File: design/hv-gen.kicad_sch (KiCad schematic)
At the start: 30 parts, among them Q1 Q_NMOS_DGS, Q2 2SA1213, T1 DA2033-AL, U8 TLP152TPL_E

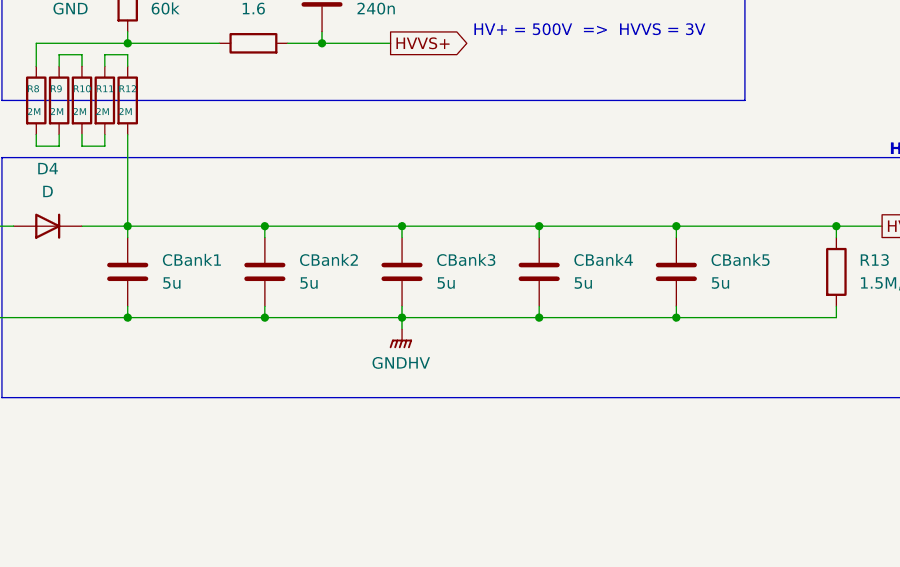
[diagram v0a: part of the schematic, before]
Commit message: fixed component value typo
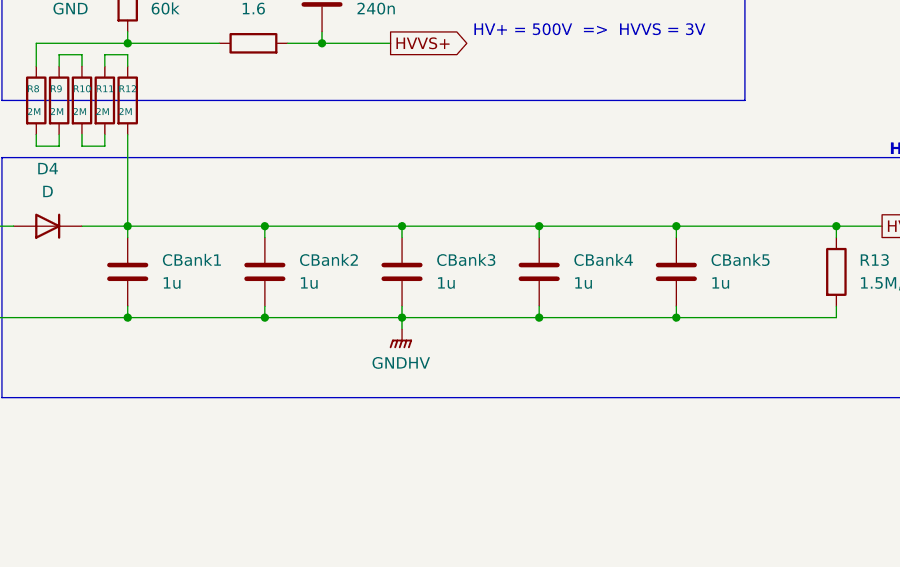
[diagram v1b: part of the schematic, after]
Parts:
- CBank1, CBank2, CBank3, CBank4, CBank5: value 5u -> 1u

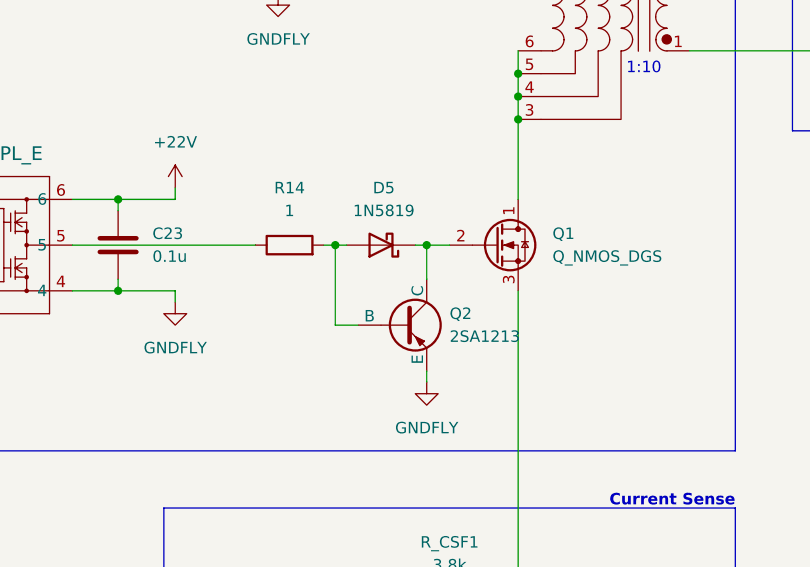
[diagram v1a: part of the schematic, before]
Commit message: Fixed PNP turnoff circuit, increased measurement buffer spacing
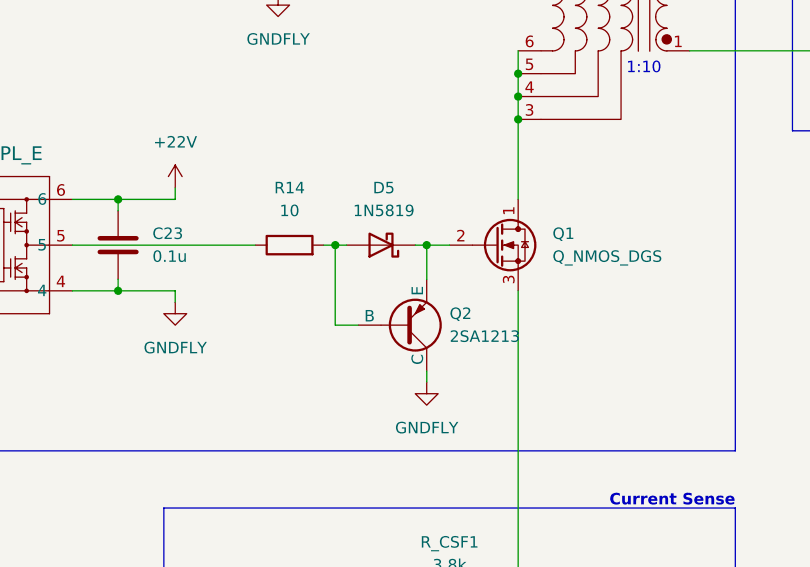
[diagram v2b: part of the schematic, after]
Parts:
- R14: value 1 -> 10; footprint Resistor_SMD:R_0603_1608Metric -> Resistor_SMD:R_0805_2012Metric
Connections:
- net GNDFLY: now also Q2.C; no longer Q2.E
- net at D5.1 (K), Q1.2 (G): now also Q2.E; no longer Q2.C

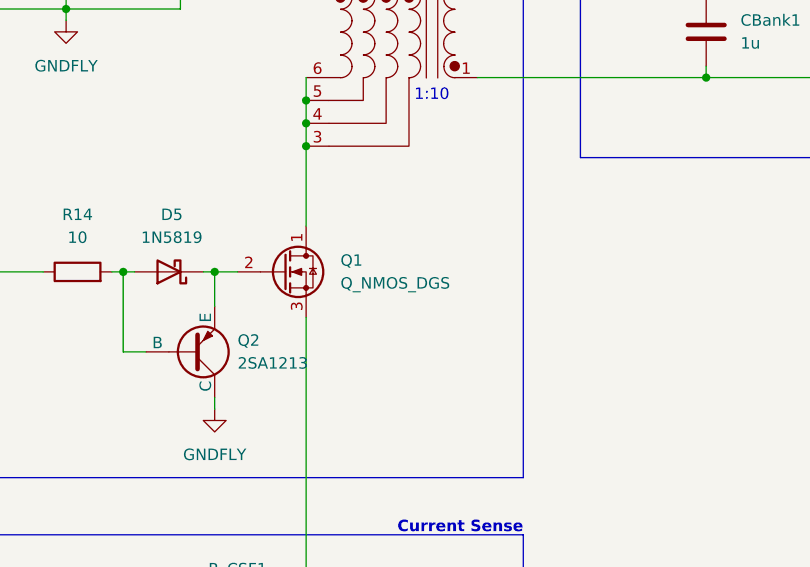
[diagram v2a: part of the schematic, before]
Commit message: corrected Q1 footprint and orientation
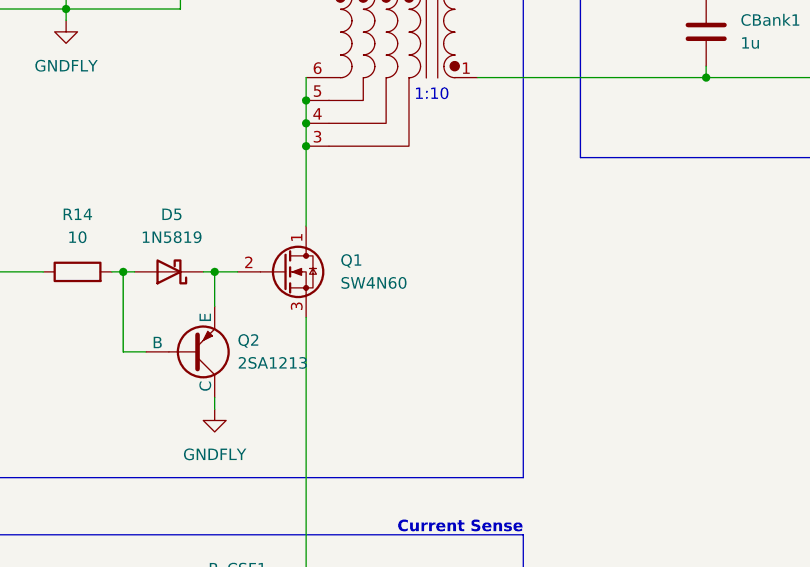
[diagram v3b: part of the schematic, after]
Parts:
- Q1: value Q_NMOS_DGS -> SW4N60; footprint Package_TO_SOT_SMD:TO-252-2 -> project-footprints:SW4N60

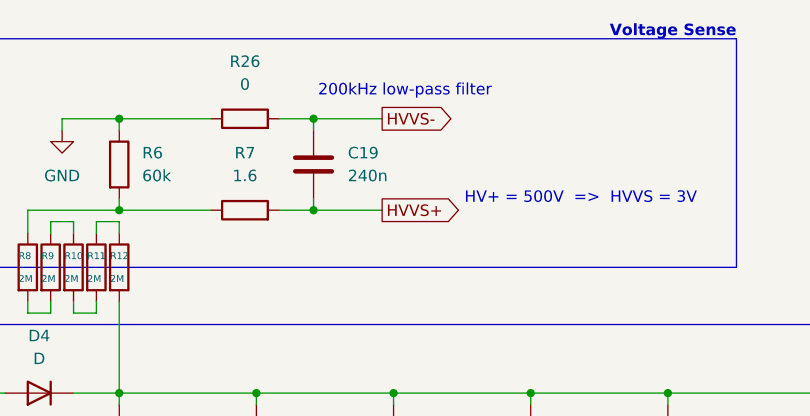
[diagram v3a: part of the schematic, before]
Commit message: Reduced HVVS filter capacitance
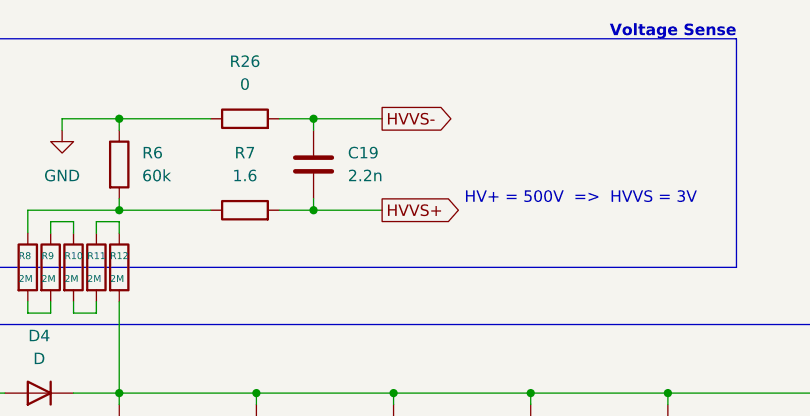
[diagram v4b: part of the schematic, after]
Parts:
- C19: value 240n -> 2.2n
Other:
- note removed: "200kHz low-pass filter"

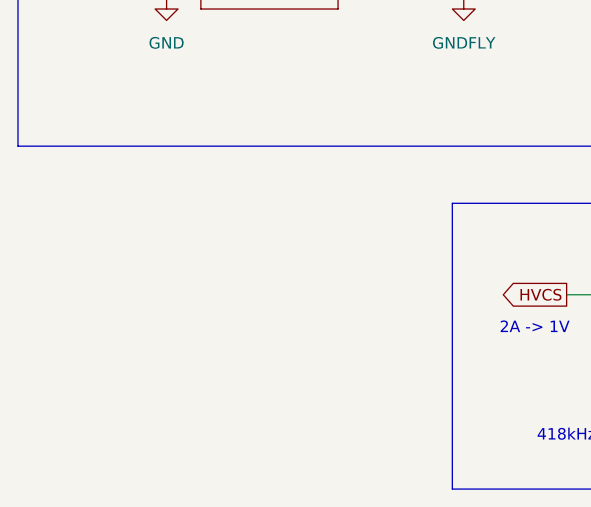
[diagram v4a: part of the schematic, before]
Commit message: Modified high voltage gate drive circuit and layout, added net tie from GND to flyback converter GND
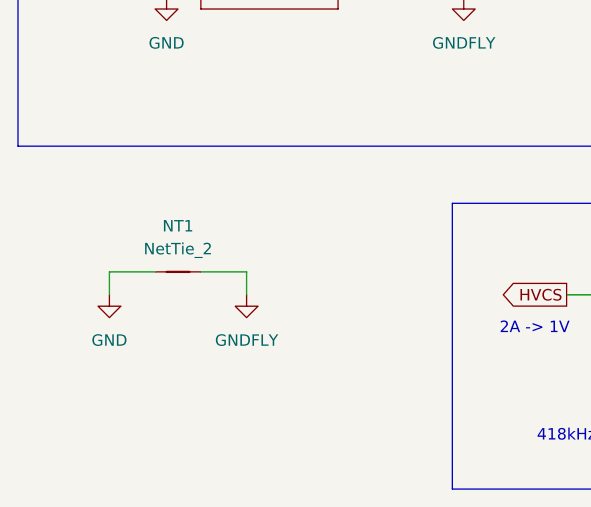
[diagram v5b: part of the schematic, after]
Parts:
- added NT1: NetTie_2, NetTie:NetTie-2_SMD_Pad2.0mm, symbol Device:NetTie_2
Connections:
- net GND: now also NT1.1
- net GNDFLY: now also NT1.2

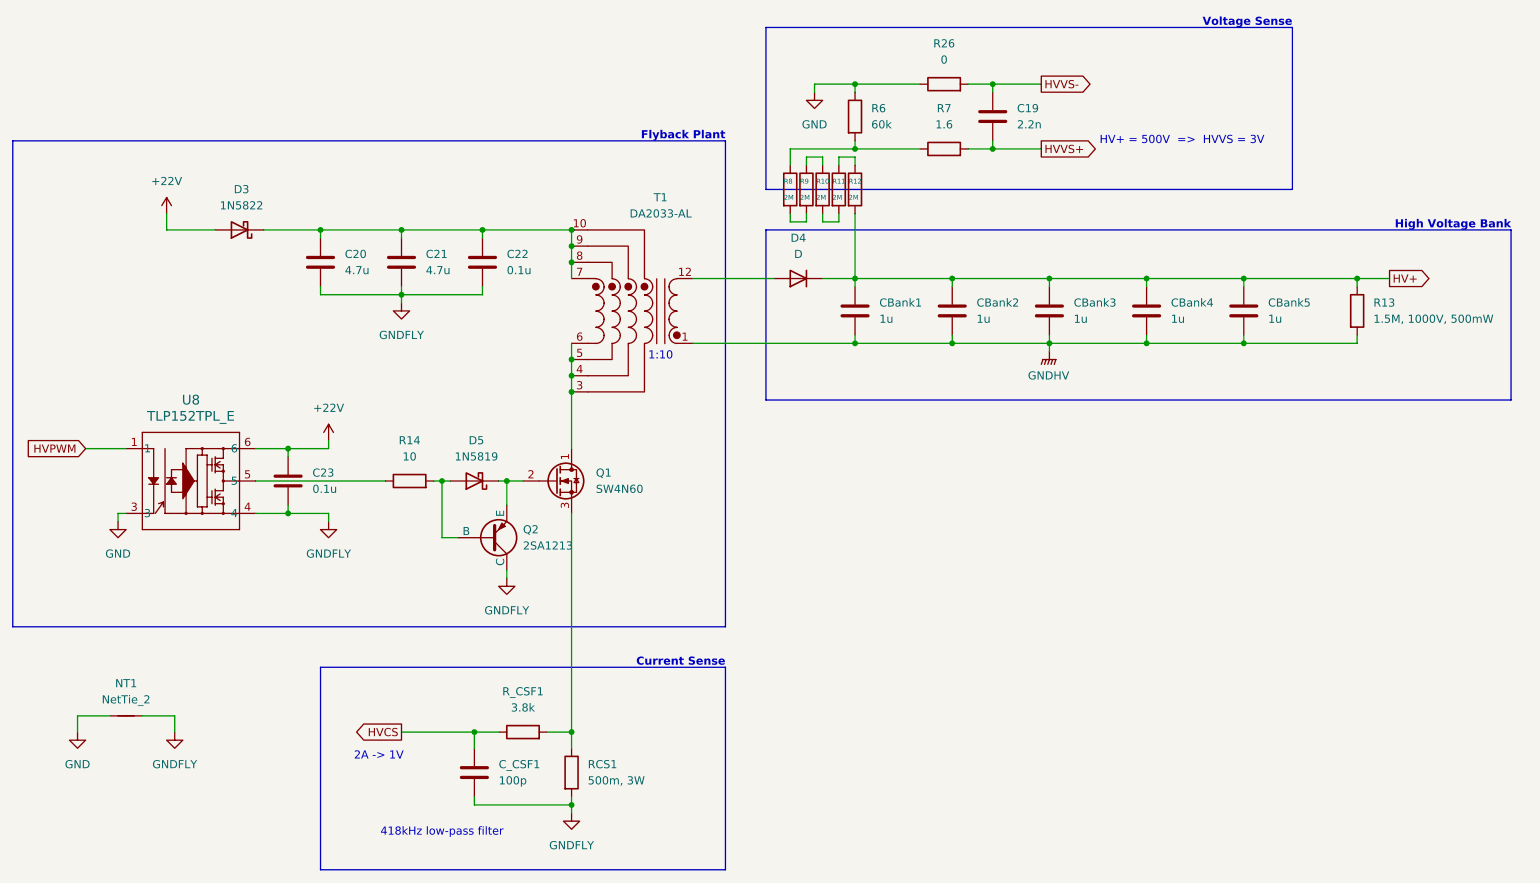
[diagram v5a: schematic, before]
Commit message: Altered HVCS filter, replaced some high current traces with filled zones, added labels
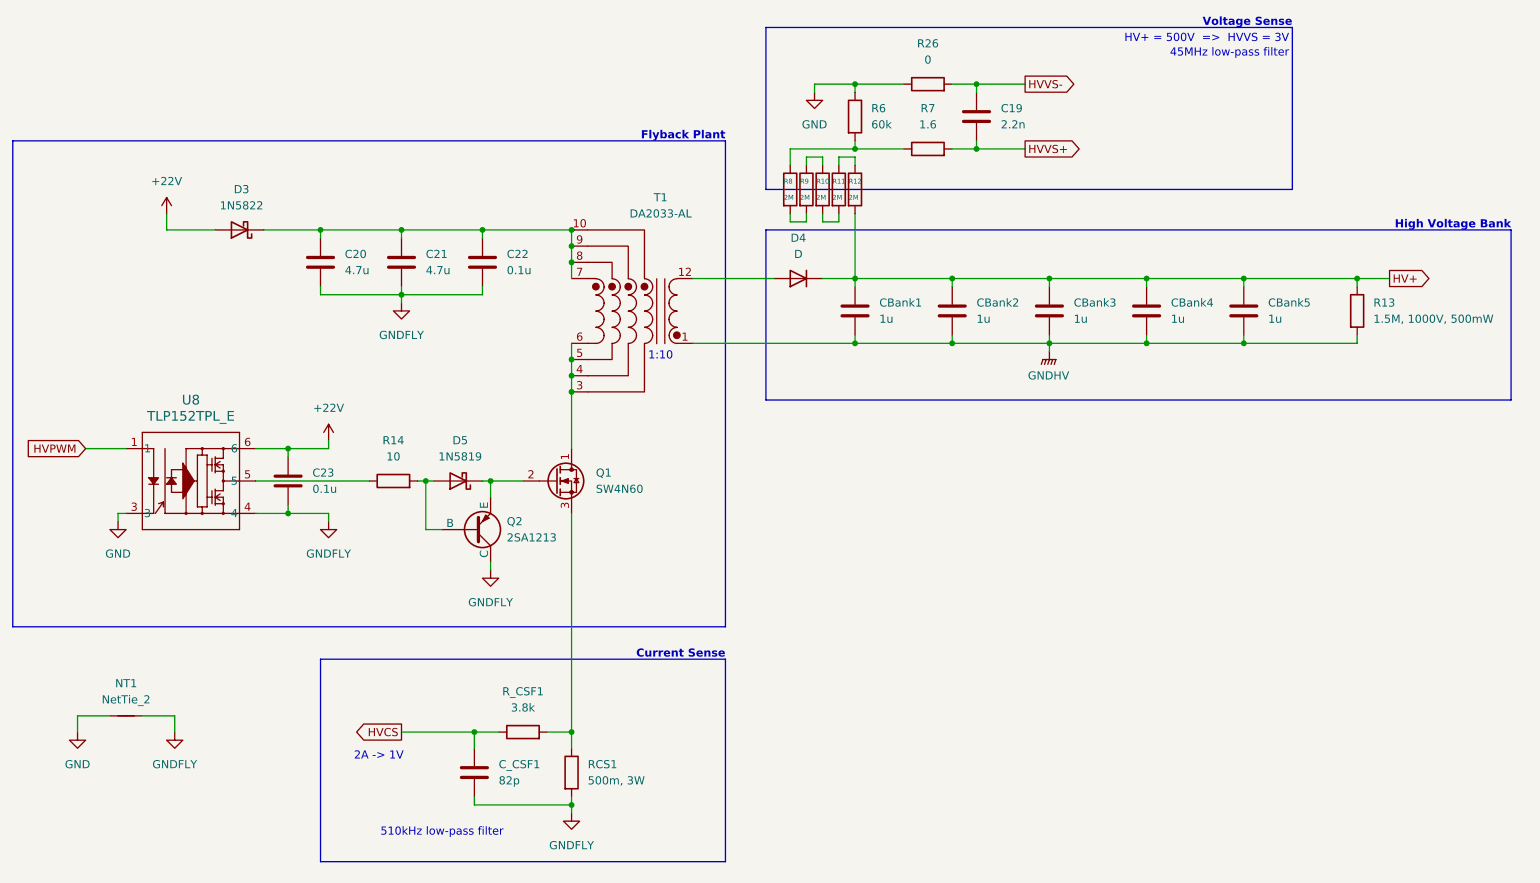
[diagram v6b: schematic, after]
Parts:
- C19: footprint Capacitor_SMD:C_0402_1005Metric -> Capacitor_SMD:C_0603_1608Metric
- C_CSF1: value 100p -> 82p
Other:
- note added: "45MHz low-pass filter"
- note added: "510kHz low-pass filter"
- note removed: "418kHz low-pass filter"
- moved on the sheet: C19, D5, Q2, R14, R26, R7

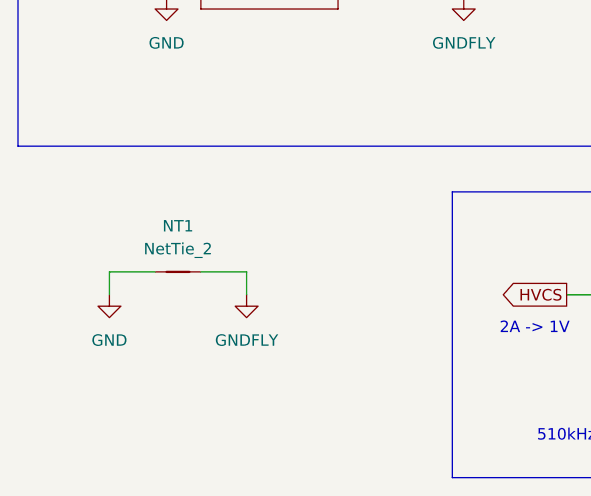
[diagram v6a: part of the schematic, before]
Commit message: added ferrite bead between HVGND and GND
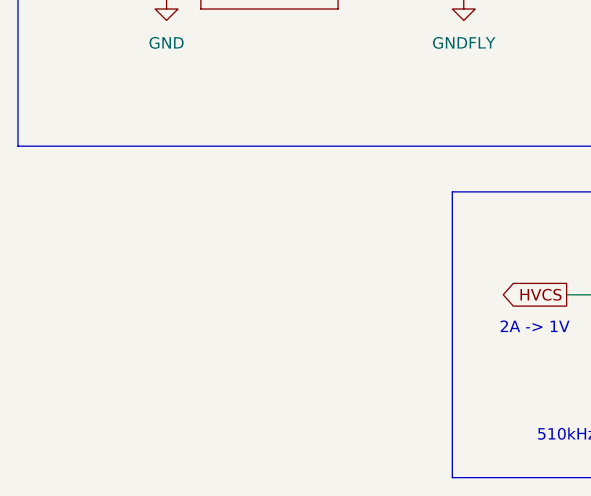
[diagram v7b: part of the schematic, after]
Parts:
- removed NT1: NetTie_2, NetTie:NetTie-2_SMD_Pad2.0mm, symbol Device:NetTie_2
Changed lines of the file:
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@@
 (kicad_sch
-	(version 20250114)
+	(version 20260306)
 	(generator "eeschema")
-	(generator_version "9.0")
+	(generator_version "10.0")
 	(paper "A4")
 	(title_block

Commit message: _
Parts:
- C23: footprint Capacitor_SMD:C_0402_1005Metric -> Capacitor_SMD:C_1206_3216Metric
